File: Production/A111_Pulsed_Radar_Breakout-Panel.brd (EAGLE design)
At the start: 120.1 x 179.1 mm, 522 parts, among them J1 RASPBERRYPI-26-PIN-GPIO, J11 RASPBERRYPI-26-PIN-GPIO, J13 RASPBERRYPI-26-PIN-GPIO, J15 RASPBERRYPI-26-PIN-GPIO, J17 RASPBERRYPI-26-PIN-GPIO, J19 RASPBERRYPI-26-PIN-GPIO, J21 RASPBERRYPI-26-PIN-GPIO, J23 RASPBERRYPI-26-PIN-GPIO, J4 RASPBERRYPI-26-PIN-GPIO, J5 RASPBERRYPI-26-PIN-GPIO, J7 RASPBERRYPI-26-PIN-GPIO, J9 RASPBERRYPI-26-PIN-GPIO, U1 A111, U10 A111, U11 1.8V, U12 TXB0108DQSR, U13 A111, U14 1.8V, U15 TXB0108DQSR, U16 A111, U17 1.8V, U18 TXB0108DQSR, U19 A111, U2 1.8V, U20 1.8V, U21 TXB0108DQSR, U22 A111, U23 1.8V, U24 TXB0108DQSR, U25 A111, U26 1.8V, U27 TXB0108DQSR, U28 A111, U29 1.8V, U3 A111, U30 TXB0108DQSR, U31 A111, U32 1.8V, U33 TXB0108DQSR, U34 A111, U35 1.8V, U36 TXB0108DQSR, U4 TXB0108DQSR, U5 1.8V, U6 TXB0108DQSR, U7 A111, U8 1.8V, U9 TXB0108DQSR, Y1 26MHz, Y10 26MHz, Y11 26MHz, Y12 26MHz, Y2 26MHz, Y3 26MHz, Y4 26MHz, Y5 26MHz, Y6 26MHz, Y7 26MHz, Y8 26MHz, Y9 26MHz

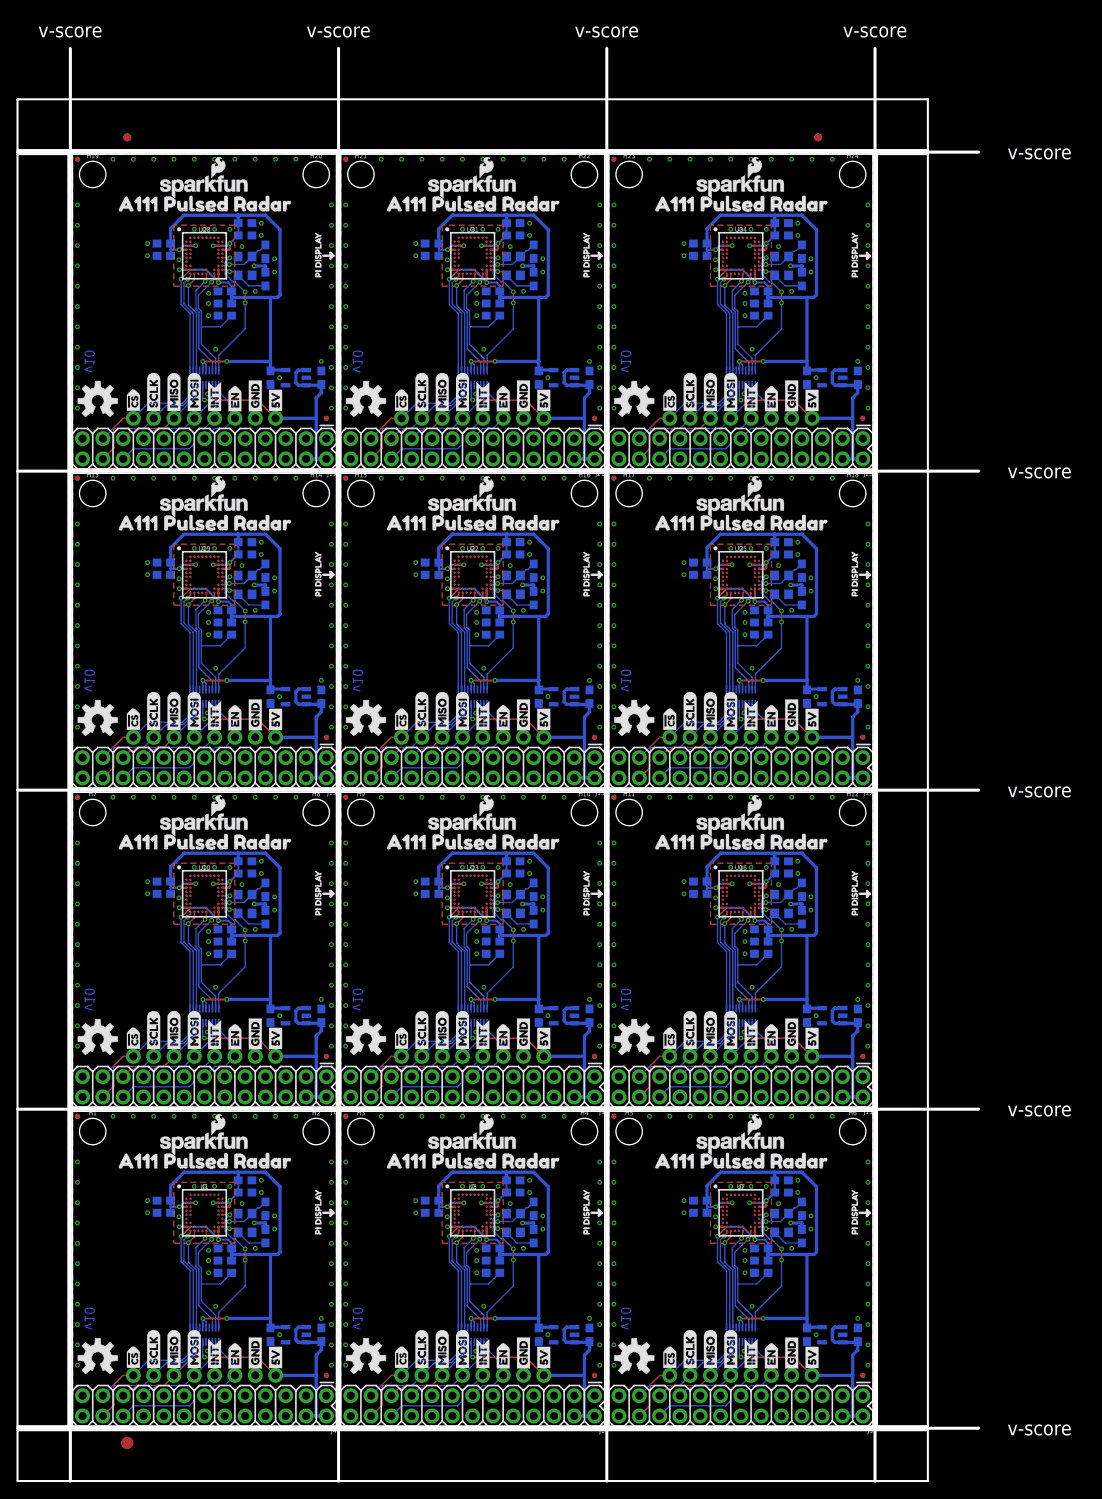
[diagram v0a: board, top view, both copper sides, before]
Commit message: Updates the panel
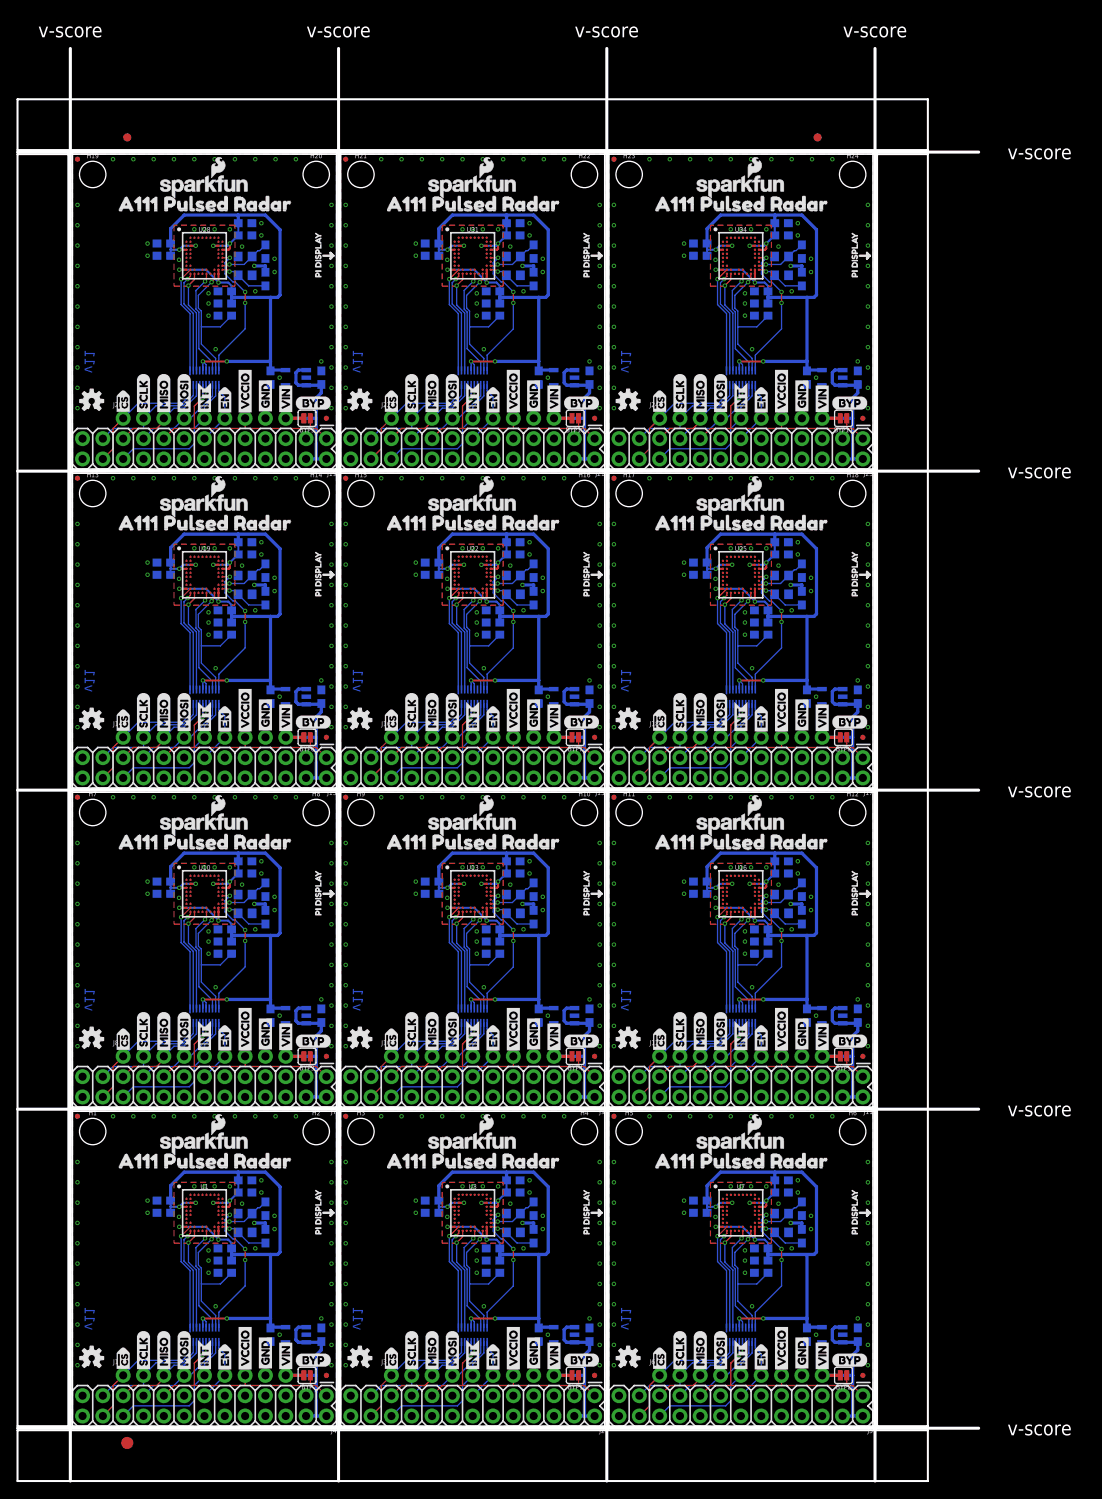
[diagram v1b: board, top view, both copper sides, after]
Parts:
- added BYP, BYP1, BYP10, BYP11, BYP2, BYP3, BYP4, BYP5, BYP6, BYP7, BYP8, BYP9: JUMPER-SMT_2_NO_SILK, SparkFun-Jumpers:SMT-JUMPER_2_NO_SILK
- added U$205, U$225: (no value), buzzard_labels:GND0
- added U$206, U$221, U$226: (no value), buzzard_labels:SCLK3
- added U$207, U$222, U$227: (no value), buzzard_labels:MISO4
- added U$208, U$212, U$228, U$232: (no value), buzzard_labels:#CS9
- added U$209, U$210, U$229, U$230: (no value), buzzard_labels:A111_PULSED_RADAR9
- added U$211, U$231: (no value), buzzard_labels:PI_DISPLAY9
- added U$213, U$214, U$233, U$234: (no value), buzzard_labels:EN9
- added U$215, U$235: (no value), SparkFun-Buzzard:BYP
- added U$216, U$236: (no value), buzzard_labels-x02:VIN0
- added U$217, U$218, U$237, U$238: (no value), buzzard_labels-x02:VCCIO1
- added U$219, U$239: (no value), buzzard_labels-x02:VIN5
- added U$220, U$240: (no value), buzzard_labels-x02:GND6
- added U$223: (no value), buzzard_labels:MOSI5
- added U$224: (no value), buzzard_labels:INT8
- J1: value RASPBERRYPI-26-PIN-GPIO -> (none); device SparkFun-Connectors:2X13 -> SparkFun-Connectors:1X09_NO_SILK
- J10, J12, J14, J16, J18, J20, J22, J24, J3, J6, J8: device SparkFun-Connectors:1X08_NO_SILK -> SparkFun-Connectors:1X09_NO_SILK
- J2: value (none) -> RASPBERRYPI-26-PIN-GPIO; device SparkFun-Connectors:1X08_NO_SILK -> SparkFun-Connectors:2X13
- LOGO10, LOGO13, LOGO16, LOGO19, LOGO2, LOGO22, LOGO25, LOGO28, LOGO31, LOGO34, LOGO4, LOGO7: value OSHW-LOGOM -> OSHW-LOGOS; device SparkFun-Aesthetics:OSHW-LOGO-M -> SparkFun-Aesthetics:OSHW-LOGO-S
- U$100: device buzzard_labels:#CS9 -> buzzard_labels-x02:GND6
- U$101, U$186: device buzzard_labels:EN9 -> buzzard_labels:SCLK3
- U$102, U$187, U$67: device buzzard_labels:EN9 -> buzzard_labels:MISO4
- U$103, U$143: device buzzard_labels:SCLK3 -> buzzard_labels:MOSI5
- U$104, U$144: device buzzard_labels:MISO4 -> buzzard_labels:INT8
- U$105: device buzzard_labels:MOSI5 -> buzzard_labels:GND0
- U$106: device buzzard_labels:INT8 -> buzzard_labels:SCLK3
- U$107, U$15, U$162: device buzzard_labels:GND0 -> buzzard_labels:MISO4
- U$108, U$112: device buzzard_labels:5V1 -> buzzard_labels:#CS9
- U$109, U$69: device buzzard_labels:SCLK3 -> buzzard_labels:A111_PULSED_RADAR9
- U$110, U$189, U$70: device buzzard_labels:MISO4 -> buzzard_labels:A111_PULSED_RADAR9
- U$111: device buzzard_labels:GND0 -> buzzard_labels:PI_DISPLAY9
- U$113, U$134: device buzzard_labels:#CS9 -> buzzard_labels:EN9
- U$114: device buzzard_labels:A111_PULSED_RADAR9 -> buzzard_labels:EN9
- U$115: device buzzard_labels:A111_PULSED_RADAR9 -> SparkFun-Buzzard:BYP
- U$116: device buzzard_labels:PI_DISPLAY9 -> buzzard_labels-x02:VIN0
- U$117, U$198: device buzzard_labels:#CS9 -> buzzard_labels-x02:VCCIO1
- U$118: device buzzard_labels:EN9 -> buzzard_labels-x02:VCCIO1
- U$119: device buzzard_labels:EN9 -> buzzard_labels-x02:VIN5
- U$120, U$160: device buzzard_labels:SCLK3 -> buzzard_labels-x02:GND6
- U$121, U$161: device buzzard_labels:MISO4 -> buzzard_labels:SCLK3
- U$122: device buzzard_labels:MOSI5 -> buzzard_labels:MISO4
- U$123: device buzzard_labels:INT8 -> buzzard_labels:MOSI5
- U$124: device buzzard_labels:GND0 -> buzzard_labels:INT8
- U$125: device buzzard_labels:5V1 -> buzzard_labels:GND0
- U$128, U$192: device buzzard_labels:GND0 -> buzzard_labels:#CS9
- U$129: device buzzard_labels:5V1 -> buzzard_labels:A111_PULSED_RADAR9
- U$130, U$49: device buzzard_labels:#CS9 -> buzzard_labels:A111_PULSED_RADAR9
- U$131: device buzzard_labels:A111_PULSED_RADAR9 -> buzzard_labels:PI_DISPLAY9
- U$132, U$148: device buzzard_labels:A111_PULSED_RADAR9 -> buzzard_labels:#CS9
- U$133: device buzzard_labels:PI_DISPLAY9 -> buzzard_labels:EN9
- U$135: device buzzard_labels:EN9 -> SparkFun-Buzzard:BYP
- U$136: device buzzard_labels:EN9 -> buzzard_labels-x02:VIN0
- U$137, U$177, U$58: device buzzard_labels:SCLK3 -> buzzard_labels-x02:VCCIO1
- U$138, U$178, U$19: device buzzard_labels:MISO4 -> buzzard_labels-x02:VCCIO1
- U$139: device buzzard_labels:MOSI5 -> buzzard_labels-x02:VIN5
- U$140, U$21: device buzzard_labels:INT8 -> buzzard_labels-x02:GND6
- U$141, U$26: device buzzard_labels:GND0 -> buzzard_labels:SCLK3
- U$142, U$27: device buzzard_labels:5V1 -> buzzard_labels:MISO4
- U$146, U$61: device buzzard_labels:5V1 -> buzzard_labels:SCLK3
- U$147, U$202, U$62: device buzzard_labels:#CS9 -> buzzard_labels:MISO4
- U$150: device buzzard_labels:PI_DISPLAY9 -> buzzard_labels:A111_PULSED_RADAR9
- U$151: device buzzard_labels:#CS9 -> buzzard_labels:PI_DISPLAY9
- U$152, U$68: device buzzard_labels:EN9 -> buzzard_labels:#CS9
- U$154, U$194: device buzzard_labels:SCLK3 -> buzzard_labels:EN9
- U$155, U$195: device buzzard_labels:MISO4 -> SparkFun-Buzzard:BYP
- U$156: device buzzard_labels:MOSI5 -> buzzard_labels-x02:VIN0
- U$157, U$38: device buzzard_labels:INT8 -> buzzard_labels-x02:VCCIO1
- U$158, U$77: device buzzard_labels:GND0 -> buzzard_labels-x02:VCCIO1
- U$159: device buzzard_labels:5V1 -> buzzard_labels-x02:VIN5
- U$16, U$176: device buzzard_labels:5V1 -> buzzard_labels-x02:VIN0
- U$163, U$23: device buzzard_labels:5V1 -> buzzard_labels:MOSI5
- U$164: device buzzard_labels:#CS9 -> buzzard_labels:INT8
- U$165: device buzzard_labels:A111_PULSED_RADAR9 -> buzzard_labels:GND0
- U$166, U$46, U$81: device buzzard_labels:A111_PULSED_RADAR9 -> buzzard_labels:SCLK3
- U$167, U$82: device buzzard_labels:PI_DISPLAY9 -> buzzard_labels:MISO4
- U$169, U$170, U$50: device buzzard_labels:EN9 -> buzzard_labels:A111_PULSED_RADAR9
- U$171: device buzzard_labels:SCLK3 -> buzzard_labels:PI_DISPLAY9
- U$172: device buzzard_labels:MISO4 -> buzzard_labels:#CS9
- U$173, U$54: device buzzard_labels:MOSI5 -> buzzard_labels:EN9
- U$174: device buzzard_labels:INT8 -> buzzard_labels:EN9
- U$175: device buzzard_labels:GND0 -> SparkFun-Buzzard:BYP
- U$179, U$22, U$39: device buzzard_labels:GND0 -> buzzard_labels-x02:VIN5
- U$180, U$40: device buzzard_labels:5V1 -> buzzard_labels-x02:GND6
- U$181, U$66: device buzzard_labels:#CS9 -> buzzard_labels:SCLK3
- U$182, U$47: device buzzard_labels:A111_PULSED_RADAR9 -> buzzard_labels:MISO4
- U$183, U$63: device buzzard_labels:A111_PULSED_RADAR9 -> buzzard_labels:MOSI5
- U$184: device buzzard_labels:PI_DISPLAY9 -> buzzard_labels:INT8
- U$185, U$45: device buzzard_labels:#CS9 -> buzzard_labels:GND0
- U$188, U$52, U$92: device buzzard_labels:SCLK3 -> buzzard_labels:#CS9
- U$190: device buzzard_labels:MOSI5 -> buzzard_labels:A111_PULSED_RADAR9
- U$191: device buzzard_labels:INT8 -> buzzard_labels:PI_DISPLAY9
- U$193, U$74: device buzzard_labels:5V1 -> buzzard_labels:EN9
- U$196, U$56: device buzzard_labels:GND0 -> buzzard_labels-x02:VIN0
- U$197, U$57, U$78: device buzzard_labels:5V1 -> buzzard_labels-x02:VCCIO1
- U$199: device buzzard_labels:A111_PULSED_RADAR9 -> buzzard_labels-x02:VIN5
- U$20, U$37: device buzzard_labels:MOSI5 -> buzzard_labels-x02:VCCIO1
- U$200, U$80: device buzzard_labels:A111_PULSED_RADAR9 -> buzzard_labels-x02:GND6
- U$201: device buzzard_labels:PI_DISPLAY9 -> buzzard_labels:SCLK3
- U$203: device buzzard_labels:EN9 -> buzzard_labels:MOSI5
- U$204, U$84: device buzzard_labels:EN9 -> buzzard_labels:INT8
- U$24: device buzzard_labels:SCLK3 -> buzzard_labels:INT8
- U$25: device buzzard_labels:MISO4 -> buzzard_labels:GND0
- U$35, U$75: device buzzard_labels:SCLK3 -> SparkFun-Buzzard:BYP
- U$36, U$76: device buzzard_labels:MISO4 -> buzzard_labels-x02:VIN0
- U$43: device buzzard_labels:GND0 -> buzzard_labels:MOSI5
- U$44: device buzzard_labels:5V1 -> buzzard_labels:INT8
- U$48: device buzzard_labels:PI_DISPLAY9 -> buzzard_labels:#CS9
- U$51: device buzzard_labels:EN9 -> buzzard_labels:PI_DISPLAY9
- U$53, U$93: device buzzard_labels:MISO4 -> buzzard_labels:EN9
- U$55: device buzzard_labels:INT8 -> SparkFun-Buzzard:BYP
- U$59: device buzzard_labels:MISO4 -> buzzard_labels-x02:VIN5
- U$60: device buzzard_labels:GND0 -> buzzard_labels-x02:GND6
- U$64: device buzzard_labels:A111_PULSED_RADAR9 -> buzzard_labels:INT8
- U$65: device buzzard_labels:PI_DISPLAY9 -> buzzard_labels:GND0
- U$71: device buzzard_labels:MOSI5 -> buzzard_labels:PI_DISPLAY9
- U$72: device buzzard_labels:INT8 -> buzzard_labels:#CS9
- U$73, U$94: device buzzard_labels:GND0 -> buzzard_labels:EN9
- U$79: device buzzard_labels:#CS9 -> buzzard_labels-x02:VIN5
- U$8, U$95: device buzzard_labels:5V1 -> SparkFun-Buzzard:BYP
- U$83: device buzzard_labels:#CS9 -> buzzard_labels:MOSI5
- U$85: device buzzard_labels:EN9 -> buzzard_labels:GND0
- U$88: device buzzard_labels:MOSI5 -> buzzard_labels:#CS9
- U$89: device buzzard_labels:INT8 -> buzzard_labels:A111_PULSED_RADAR9
- U$90: device buzzard_labels:GND0 -> buzzard_labels:A111_PULSED_RADAR9
- U$91: device buzzard_labels:5V1 -> buzzard_labels:PI_DISPLAY9
- U$96: device buzzard_labels:#CS9 -> buzzard_labels-x02:VIN0
- U$97, U$98: device buzzard_labels:A111_PULSED_RADAR9 -> buzzard_labels-x02:VCCIO1
- U$99: device buzzard_labels:PI_DISPLAY9 -> buzzard_labels-x02:VIN5
- U11, U14, U17, U2, U20, U23, U26, U29, U32, U35, U5, U8: value 1.8V -> AP2127K-1.8V
- moved U$165 109.4 mm to (91.2, 86.5), turned to 90 degrees
- moved U$114 105.5 mm to (86.1, 46.5), turned to 90 degrees
- moved U$115 92.5 mm to (94.9, 48.1), flipped to the top
- moved U$117 90.3 mm to (88.6, 46.5)
- moved U$59 90.3 mm to (93.7, 6.73)
- moved U$58 88.1 mm to (88.6, 6.60), flipped to the top
- moved U$113 88.0 mm to (86.1, 46.5), flipped to the bottom
- moved U$55 86.1 mm to (94.9, 8.26), turned to 0 degrees
- moved U$105 85.8 mm to (91.2, 46.6)
- moved U$164 85.8 mm to (83.6, 86.4)
- moved U$116 84.6 mm to (93.7, 46.5)
- moved U$110 84.3 mm to (95.9, 73.0), turned to 0 degrees
- moved U$53 83.6 mm to (86.1, 6.60), flipped to the bottom
- moved U$192 83.6 mm to (6.35, 126.1), flipped to the bottom
- moved U$119 83.5 mm to (93.7, 46.6), flipped to the bottom
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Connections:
- removed net 5V: C9.1, J2.1, J4.2, J4.4, U2.1, U2.3, U4.16
- removed net 5V1: C19.1, J1.2, J1.4, J3.1, U5.1, U5.3, U6.16
- removed net 5V10: C109.1, J21.2, J21.4, J22.1, U32.1, U32.3, U33.16
- removed net 5V11: C119.1, J23.2, J23.4, J24.1, U35.1, U35.3, U36.16
- removed net 5V2: C29.1, J5.2, J5.4, J6.1, U8.1, U8.3, U9.16
- removed net 5V3: C39.1, J7.2, J7.4, J8.1, U11.1, U11.3, U12.16
- removed net 5V4: C49.1, J10.1, J9.2, J9.4, U14.1, U14.3, U15.16
- removed net 5V5: C59.1, J11.2, J11.4, J12.1, U17.1, U17.3, U18.16
- removed net 5V6: C69.1, J13.2, J13.4, J14.1, U20.1, U20.3, U21.16
- removed net 5V7: C79.1, J15.2, J15.4, J16.1, U23.1, U23.3, U24.16
- removed net 5V8: C89.1, J17.2, J17.4, J18.1, U26.1, U26.3, U27.16
- removed net 5V9: C99.1, J19.2, J19.4, J20.1, U29.1, U29.3, U30.16
- new net VCCIO: BYP.1, J1.7, J4.1, J4.17, U4.16
- new net VCCIO1: BYP1.1, J2.1, J2.17, J3.7, U6.16
- new net VCCIO10: BYP10.1, J21.1, J21.17, J22.7, U33.16
- new net VCCIO11: BYP11.1, J23.1, J23.17, J24.7, U36.16
- new net VCCIO2: BYP2.1, J5.1, J5.17, J6.7, U9.16
- new net VCCIO3: BYP3.1, J7.1, J7.17, J8.7, U12.16
- new net VCCIO4: BYP4.1, J10.7, J9.1, J9.17, U15.16
- new net VCCIO5: BYP5.1, J11.1, J11.17, J12.7, U18.16
- new net VCCIO6: BYP6.1, J13.1, J13.17, J14.7, U21.16
- new net VCCIO7: BYP7.1, J15.1, J15.17, J16.7, U24.16
- new net VCCIO8: BYP8.1, J17.1, J17.17, J18.7, U27.16
- new net VCCIO9: BYP9.1, J19.1, J19.17, J20.7, U30.16
- new net VIN: BYP.2, C9.1, J1.9, J4.2, J4.4, U2.1, U2.3
- new net VIN1: BYP1.2, C19.1, J2.2, J2.4, J3.9, U5.1, U5.3
- new net VIN10: BYP10.2, C109.1, J21.2, J21.4, J22.9, U32.1, U32.3
- new net VIN11: BYP11.2, C119.1, J23.2, J23.4, J24.9, U35.1, U35.3
- new net VIN2: BYP2.2, C29.1, J5.2, J5.4, J6.9, U8.1, U8.3
- new net VIN3: BYP3.2, C39.1, J7.2, J7.4, J8.9, U11.1, U11.3
- new net VIN4: BYP4.2, C49.1, J10.9, J9.2, J9.4, U14.1, U14.3
- new net VIN5: BYP5.2, C59.1, J11.2, J11.4, J12.9, U17.1, U17.3
- new net VIN6: BYP6.2, C69.1, J13.2, J13.4, J14.9, U20.1, U20.3
- new net VIN7: BYP7.2, C79.1, J15.2, J15.4, J16.9, U23.1, U23.3
- new net VIN8: BYP8.2, C89.1, J17.2, J17.4, J18.9, U26.1, U26.3
- new net VIN9: BYP9.2, C99.1, J19.2, J19.4, J20.9, U29.1, U29.3
- net !CS!_RPI: now also J1.1; no longer J2.8
- net !CS!_RPI1: now also J2.24, J3.1; no longer J1.24, J3.8
- net !CS!_RPI10: now also J22.1; no longer J22.8
- net !CS!_RPI11: now also J24.1; no longer J24.8
- net !CS!_RPI2: now also J6.1; no longer J6.8
- net !CS!_RPI3: now also J8.1; no longer J8.8
- net !CS!_RPI4: now also J10.1; no longer J10.8
- net !CS!_RPI5: now also J12.1; no longer J12.8
- net !CS!_RPI6: now also J14.1; no longer J14.8
- net !CS!_RPI7: now also J16.1; no longer J16.8
- net !CS!_RPI8: now also J18.1; no longer J18.8
- net !CS!_RPI9: now also J20.1; no longer J20.8
- net ENABLE_RPI: now also J1.6; no longer J2.3
- net ENABLE_RPI1: now also J2.13, J3.6; no longer J1.13, J3.3
- net ENABLE_RPI10: now also J22.6; no longer J22.3
- net ENABLE_RPI11: now also J24.6; no longer J24.3
- net ENABLE_RPI2: now also J6.6; no longer J6.3
- net ENABLE_RPI3: now also J8.6; no longer J8.3
- net ENABLE_RPI4: now also J10.6; no longer J10.3
- net ENABLE_RPI5: now also J12.6; no longer J12.3
- net ENABLE_RPI6: now also J14.6; no longer J14.3
- net ENABLE_RPI7: now also J16.6; no longer J16.3
- net ENABLE_RPI8: now also J18.6; no longer J18.3
- net ENABLE_RPI9: now also J20.6; no longer J20.3
- net GND: now also J1.8; no longer J2.2
- net GND1: now also J2.14, J2.20, J2.25, J2.6, J2.9, J3.8; no longer J1.14, J1.20, J1.25, J1.6, J1.9, J3.2
- net GND10: now also J22.8; no longer J22.2
- net GND11: now also J24.8; no longer J24.2
- net GND2: now also J6.8; no longer J6.2
- net GND3: now also J8.8; no longer J8.2
- net GND4: now also J10.8; no longer J10.2
- net GND5: now also J12.8; no longer J12.2
- net GND6: now also J14.8; no longer J14.2
- net GND7: now also J16.8; no longer J16.2
- net GND8: now also J18.8; no longer J18.2
- net GND9: now also J20.8; no longer J20.2
- net INTERRUPT_RPI: now also J1.5; no longer J2.4
- net INTERRUPT_RPI1: now also J2.22, J3.5; no longer J1.22, J3.4
- net INTERRUPT_RPI10: now also J22.5; no longer J22.4
- net INTERRUPT_RPI11: now also J24.5; no longer J24.4
- net INTERRUPT_RPI2: now also J6.5; no longer J6.4
- net INTERRUPT_RPI3: now also J8.5; no longer J8.4
- net INTERRUPT_RPI4: now also J10.5; no longer J10.4
- net INTERRUPT_RPI5: now also J12.5; no longer J12.4
- net INTERRUPT_RPI6: now also J14.5; no longer J14.4
- net INTERRUPT_RPI7: now also J16.5; no longer J16.4
- net INTERRUPT_RPI8: now also J18.5; no longer J18.4
- net INTERRUPT_RPI9: now also J20.5; no longer J20.4
- net MISO_RPI: now also J1.3; no longer J2.6
- net MISO_RPI1: now also J2.21, J3.3; no longer J1.21, J3.6
- net MISO_RPI10: now also J22.3; no longer J22.6
- net MISO_RPI11: now also J24.3; no longer J24.6
- net MISO_RPI2: now also J6.3; no longer J6.6
- net MISO_RPI3: now also J8.3; no longer J8.6
- net MISO_RPI4: now also J10.3; no longer J10.6
- net MISO_RPI5: now also J12.3; no longer J12.6
- net MISO_RPI6: now also J14.3; no longer J14.6
- net MISO_RPI7: now also J16.3; no longer J16.6
- net MISO_RPI8: now also J18.3; no longer J18.6
- net MISO_RPI9: now also J20.3; no longer J20.6
- net MOSI_RPI: now also J1.4; no longer J2.5
- net MOSI_RPI1: now also J2.19, J3.4; no longer J1.19, J3.5
- net MOSI_RPI10: now also J22.4; no longer J22.5
- net MOSI_RPI11: now also J24.4; no longer J24.5
- net MOSI_RPI2: now also J6.4; no longer J6.5
- net MOSI_RPI3: now also J8.4; no longer J8.5
- net MOSI_RPI4: now also J10.4; no longer J10.5
- net MOSI_RPI5: now also J12.4; no longer J12.5
- net MOSI_RPI6: now also J14.4; no longer J14.5
- net MOSI_RPI7: now also J16.4; no longer J16.5
- net MOSI_RPI8: now also J18.4; no longer J18.5
- net MOSI_RPI9: now also J20.4; no longer J20.5
- net SCLK_RPI: now also J1.2; no longer J2.7
- net SCLK_RPI1: now also J2.23, J3.2; no longer J1.23, J3.7
- net SCLK_RPI10: now also J22.2; no longer J22.7
- net SCLK_RPI11: now also J24.2; no longer J24.7
- net SCLK_RPI2: now also J6.2; no longer J6.7
- net SCLK_RPI3: now also J8.2; no longer J8.7
- net SCLK_RPI4: now also J10.2; no longer J10.7
- net SCLK_RPI5: now also J12.2; no longer J12.7
- net SCLK_RPI6: now also J14.2; no longer J14.7
- net SCLK_RPI7: now also J16.2; no longer J16.7
- net SCLK_RPI8: now also J18.2; no longer J18.7
- net SCLK_RPI9: now also J20.2; no longer J20.7
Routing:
- net 5V3: track 35.1 -> 0.00 mm, vias 1 -> 0
- net 5V1: track 35.1 -> 0.00 mm, vias 1 -> 0
- net 5V: track 35.1 -> 0.00 mm, vias 1 -> 0
- net 5V9: track 35.1 -> 0.00 mm, vias 1 -> 0
- net 5V8: track 35.1 -> 0.00 mm, vias 1 -> 0
- net 5V7: track 35.1 -> 0.00 mm, vias 1 -> 0
- net 5V5: track 35.1 -> 0.00 mm, vias 1 -> 0
- net 5V4: track 35.1 -> 0.00 mm, vias 1 -> 0
- net 5V2: track 35.1 -> 0.00 mm, vias 1 -> 0
- net 5V11: track 35.1 -> 0.00 mm, vias 1 -> 0
- net 5V10: track 35.1 -> 0.00 mm, vias 1 -> 0
- net 5V6: track 35.1 -> 0.00 mm, vias 1 -> 0
- net VCCIO4: track 0.00 -> 29.8 mm, vias 0 -> 1
- net VCCIO3: track 0.00 -> 29.8 mm, vias 0 -> 1
- net VCCIO5: track 0.00 -> 29.8 mm, vias 0 -> 1
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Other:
- board text added: "v11"
- board text removed: "v10"
